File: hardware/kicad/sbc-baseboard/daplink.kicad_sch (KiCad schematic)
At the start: 15 parts, among them J601 SWD (K20), SW601 DAP RESET, U601 MK20DX128VFM5, Y601 8MHz

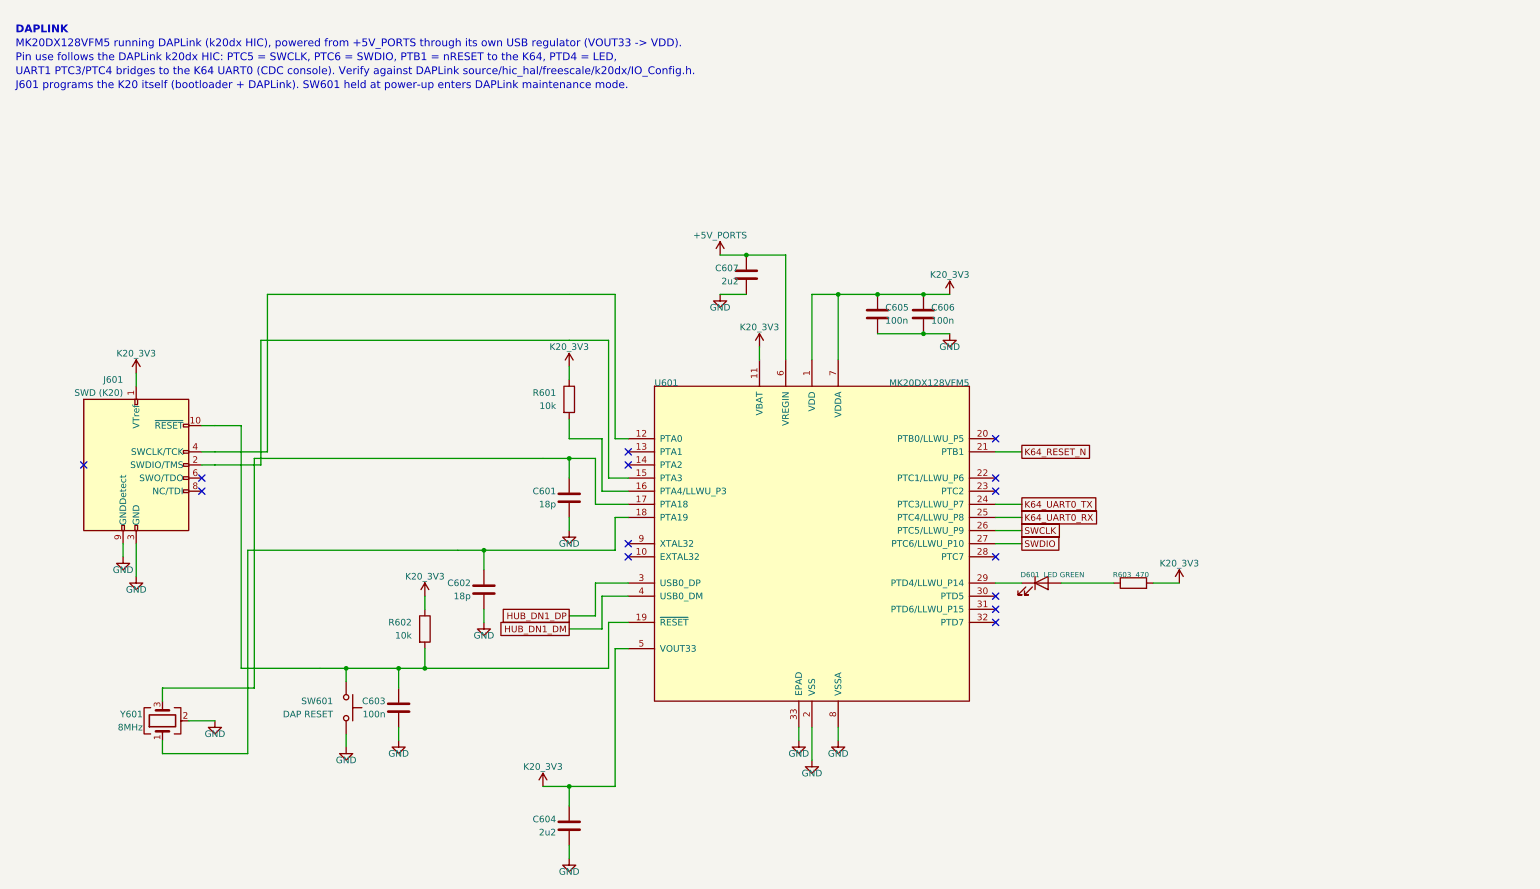
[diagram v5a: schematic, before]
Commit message: Reference-design review; pin numbers and real text widths in the layout gate
Review (docs/reference-design-review.md): every IC's surrounding parts
compared with its datasheet typical application or evaluation board.
Brought in line:
- TPS54560B compensation 16.9k / 4.7 nF / 47 pF (the 5 V / 400 kHz design
  example, same 141 uF ceramic output); the placeholders are gone.
- TPS62823 divider 453k / 100k with the 120 pF feed-forward capacitor the
  datasheet recommends.
- USB2517 VBUS_DET from the EVB: 100k / 100k with 1 uF (was 10k / 22k, 3.4 V
  at a 3.3 V pin).
- KSZ8081 MDIO pull-up 1.0k as the datasheet requires (was 4.7k).
- FT231X: 27 R in series and 47 pF on USBDM/USBDP, datasheet figure 6.1.
Deviations kept and documented: the bucks' EN gated by the PD controller
instead of a UVLO divider, the FT231X fed by a power switch instead of a
ferrite bead, translator OE tied to the target rail.

Layout gate: pin numbers are text boxes like any other, and all text widths
come from a per-glyph table fitted to the extents KiCad writes into its PDF
(check_pins.py); the generator's spacing uses the same table. That exposed
and fixed: reference/value overlaps on narrow symbols (now stacked), rail
names printed over each other (the lane end and hanging pull-up now carry
half the rail name), a port-switch value over its pin number, turned parts
with text on the pin side, lane stacks whose spread collapsed at the grid
snap, routes landing on connector pin stubs (J16, J601, J14, D202 moved),
the PD controller's I2C and gate routes that crossed half the sheet (now
labels), and the port /FAULT and I2C1 pull-ups, which as hanging resistors
staggered off the sheet and are now one column to one +3V3 symbol. The
port switch carries FAULT above OUT so the switched rail's parts hang below
the label; the VBUS row is drawn from the connector back to the switch.

All sheets: ERC 0, contacts 0, merges 0, layout 0 in every category.
Connectivity against 8579cd2 differs only in the value ch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
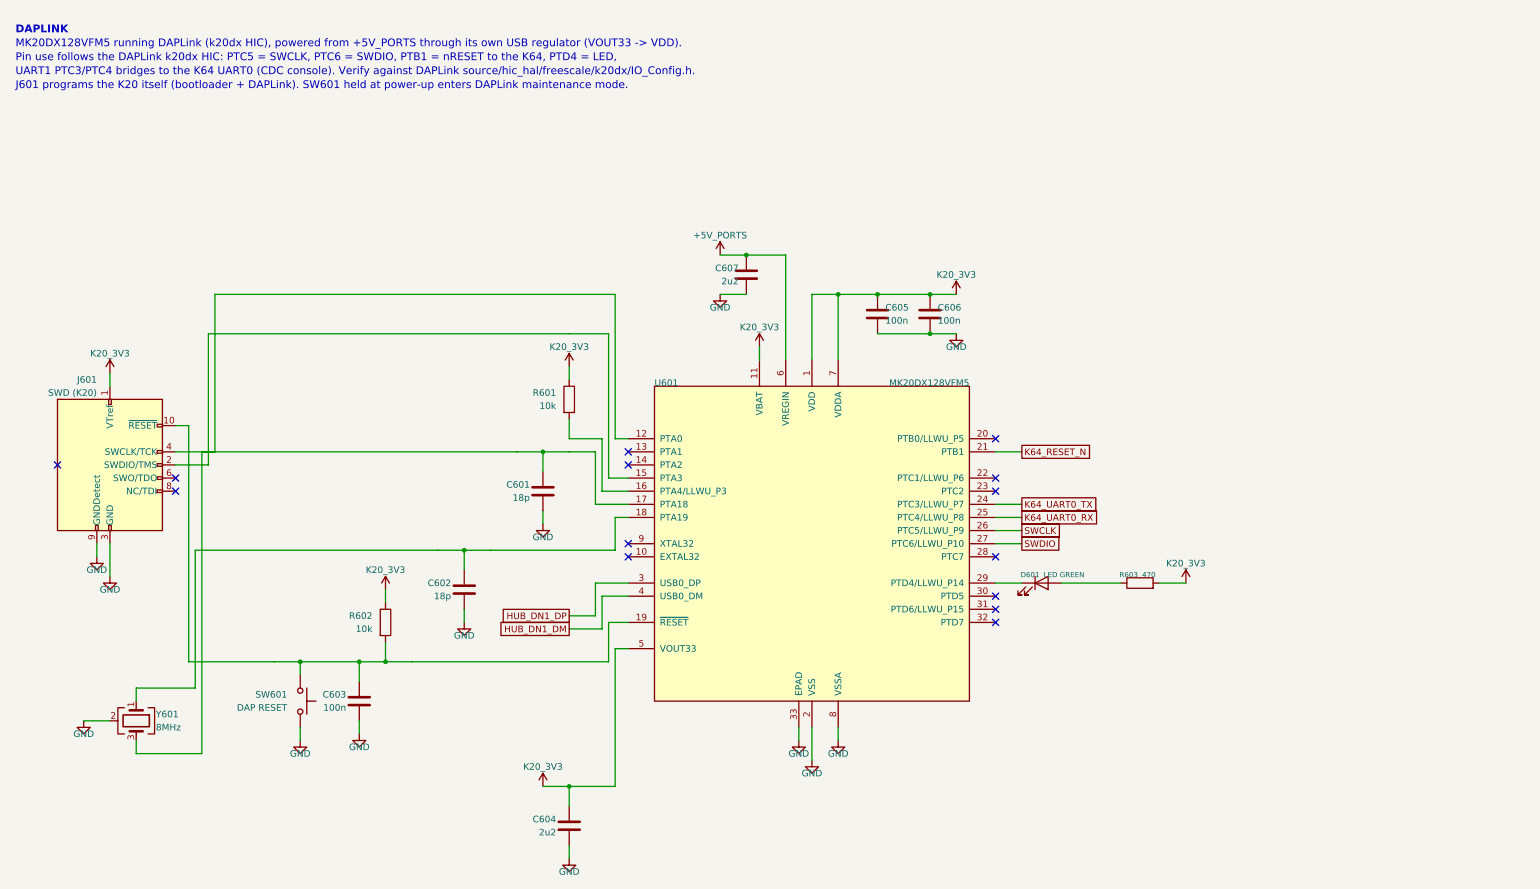
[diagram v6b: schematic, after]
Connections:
- net at C601.1, U601.17 (PTA18), Y601.3: now also J601.4 (SWCLK/TCK), U601.12 (PTA0)
